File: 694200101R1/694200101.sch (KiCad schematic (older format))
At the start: 237 parts, among them J1 USB4085-GF-A, J2 Conn_01x02_Male, J3 Conn_01x02_Male, SW1 MX_SW, SW10 MX_SW, SW100 MX_SW, SW101 MX_SW, SW102 MX_SW, SW103 MX_SW, SW104 MX_SW, SW105 MX_SW, SW106 MX_SW, SW107 MX_SW, SW11 MX_SW, SW12 MX_SW, SW13 MX_SW, SW14 MX_SW, SW15 MX_SW, SW16 MX_SW, SW17 MX_SW, SW18 MX_SW, SW19 MX_SW, SW2 MX_SW, SW20 MX_SW, SW21 MX_SW, SW22 MX_SW, SW23 MX_SW, SW24 MX_SW, SW25 MX_SW, SW26 MX_SW, SW27 MX_SW, SW28 MX_SW, SW29 MX_SW, SW3 MX_SW, SW30 MX_SW, SW31 MX_SW, SW32 MX_SW, SW33 MX_SW, SW34 MX_SW, SW35 MX_SW, SW36 MX_SW, SW37 MX_SW, SW38 MX_SW, SW39 MX_SW, SW4 MX_SW, SW40 MX_SW, SW41 MX_SW, SW42 MX_SW, SW43 MX_SW, SW44 MX_SW, SW45 MX_SW, SW46 MX_SW, SW47 MX_SW, SW48 MX_SW, SW49 MX_SW, SW5 MX_SW, SW50 MX_SW, SW51 MX_SW, SW52 MX_SW, SW53 MX_SW, SW54 MX_SW, SW55 MX_SW, SW56 MX_SW, SW57 MX_SW, SW58 MX_SW, SW59 MX_SW, SW6 MX_SW, SW60 MX_SW, SW61 MX_SW, SW62 MX_SW, SW63 MX_SW, SW64 MX_SW, SW65 MX_SW, SW66 MX_SW, SW67 MX_SW, SW68 MX_SW, SW69 MX_SW, SW7 MX_SW, SW70 MX_SW, SW71 MX_SW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

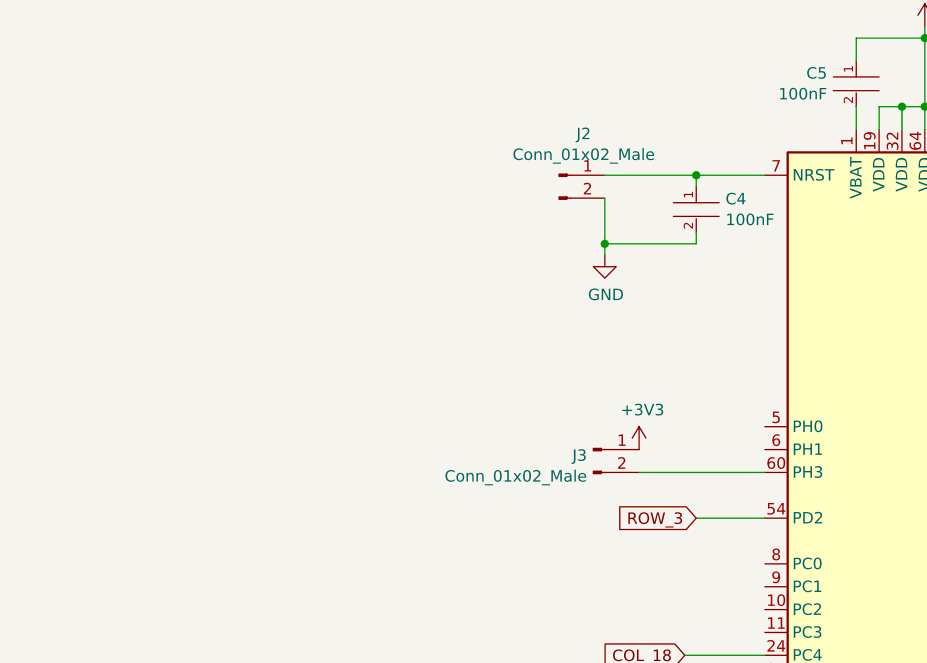
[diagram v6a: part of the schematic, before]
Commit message: Updated Schematic to use Crystal
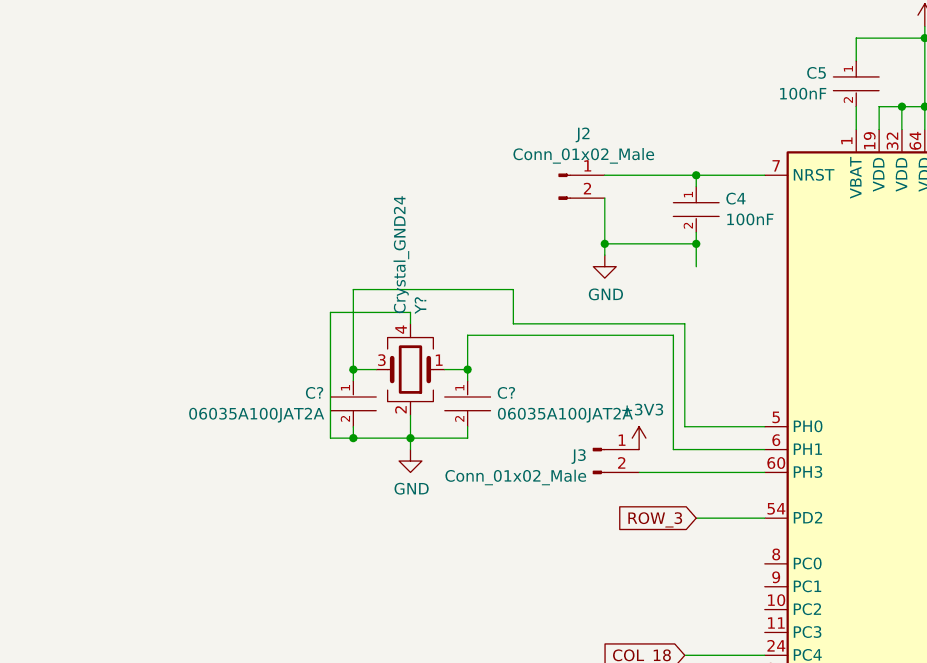
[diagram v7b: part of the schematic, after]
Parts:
- added C? (x2): 06035A100JAT2A, capacitor-lib:AVX-GRM124-0-0-IPC_C, symbol capacitor-lib:06035A100JAT2A
- added Y?: Crystal_GND24, symbol Device:Crystal_GND24
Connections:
- net GND: now also C?.2, C?.2, Y?.2, Y?.4
- net at U2.5 (PH0): now also C?.1, Y?.3
- net at U2.6 (PH1): now also C?.1, Y?.1
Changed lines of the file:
@@
 	1    0    0    -1
 $EndComp
-$Comp
-L MCU_ST_STM32L4:STM32L433RBTx U2
-U 1 1 5FE7C7AF
-P 8950 8200
-F 0 "U2" H 9200 6350 50  0000 C CNN
-F 1 "STM32L433RBTx" H 9450 6250 50  0000 C CNN
-F 2 "Package_QFP:LQFP-64_10x10mm_P0.5mm" H 8350 6500 50  0001 R CNN
-F 3 "http://www.st.com/st-web-ui/static/active/en/resource/technical/document/datasheet/DM00257192.pdf" H 8950 8200 50  0001 C CNN
-	1    8950 8200
-	1    0    0    -1
-$EndComp
 Wire Wire Line
 	8650 6100 8650 6000
@@
 	0    1    1    0
 $EndComp
-Wire Wire Line
-	9550 8900 10550 8900
-Wire Wire Line
-	9550 9000 10950 9000
 Text GLabel 11050 8900 2    50   Input ~ 0
 I2C_SCL
@@
 USB_D-
 Wire Wire Line
-	9550 7700 10000 7700
-Wire Wire Line
-	10000 7800 9550 7800
-Wire Wire Line
 	16050 6350 16050 6500
 Wire Wire Line
@@
 Text GLabel 16050 8700 3    50   Input ~ 0
 ENCODER_B
-Wire Wire Line
-	9550 8300 9900 8300
-Wire Wire Line
-	9550 8400 9900 8400
 Text GLabel 9900 8300 2    50   Input ~ 0
 ENCODER_A
@@
 Text GLabel 9900 8700 2    50   Input ~ 0
 ROW_1
-Wire Wire Line
-	9550 8800 9900 8800
-Wire Wire Line
-	9550 8700 9900 8700
-Wire Wire Line
-	9550 8600 9900 8600
 Text GLabel 9900 8600 2    50   Input ~ 0
 ROW_2
@@
 Text GLabel 7900 9300 0    50   Input ~ 0
 ROW_6
-Wire Wire Line
-	9550 8100 9900 8100
 Text GLabel 9900 8100 2    50   Input ~ 0
 COL_0
-Wire Wire Line
-	9550 8000 9900 8000
 Text GLabel 9900 8000 2    50   Input ~ 0
 COL_1
-Wire Wire Line
-	9550 7900 9900 7900
 Text GLabel 9900 7900 2    50   Input ~ 0
 COL_2
-Wire Wire Line
-	9550 7600 9900 7600
 Text GLabel 9900 7600 2    50   Input ~ 0
 COL_3
-Wire Wire Line
-	9550 7500 9900 7500
 Text GLabel 9900 7500 2    50   Input ~ 0
 COL_4
-Wire Wire Line
-	9550 7400 9900 7400
 Text GLabel 9900 7400 2    50   Input ~ 0
 COL_5
@@
 Text GLabel 7900 8900 0    50   Input ~ 0
 COL_9
-Wire Wire Line
-	9550 9800 9900 9800
 Text GLabel 9900 9800 2    50   Input ~ 0
 COL_10
-Wire Wire Line
-	9550 9700 9900 9700
 Text GLabel 9900 9700 2    50   Input ~ 0
 COL_11
-Wire Wire Line
-	9550 9600 9900 9600
 Text GLabel 9900 9600 2    50   Input ~ 0
 COL_12
-Wire Wire Line
-	9550 9500 9900 9500
 Text GLabel 9900 9500 2    50   Input ~ 0
 COL_13
-Wire Wire Line
-	9550 9400 9900 9400
 Text GLabel 9900 9400 2    50   Input ~ 0
 COL_14
-Wire Wire Line
-	9550 9300 9900 9300
 Text GLabel 9900 9300 2    50   Input ~ 0
 COL_15
-Wire Wire Line
-	9550 8500 9900 8500
 Text GLabel 9900 8500 2    50   Input ~ 0
 COL_16
@@
 Text GLabel 7900 8700 0    50   Input ~ 0
 COL_18
-Wire Wire Line
-	9550 7300 9900 7300
 Text GLabel 9900 7300 2    50   Input ~ 0
 COL_19
-Wire Wire Line
-	9550 7200 9900 7200
 Text GLabel 9900 7200 2    50   Input ~ 0
 COL_20
-Wire Wire Line
-	9550 7100 9900 7100
 Text GLabel 9900 7100 2    50   Input ~ 0
 COL_21
-Wire Wire Line
-	9550 7000 9900 7000
 Text GLabel 9900 7000 2    50   Input ~ 0
 COL_22
@@
 Wire Wire Line
 	4500 7550 4500 7500
+$Comp
+L capacitor-lib:06035A100JAT2A C?
+U 1 1 5FF44365
+P 6950 7700
+F 0 "C?" H 6822 7554 50  0000 R CNN
+F 1 "06035A100JAT2A" H 6822 7645 50  0000 R CNN
+F 2 "capacitor-lib:AVX-GRM124-0-0-IPC_C" H 6950 8000 50  0001 L CNN
+F 3 "https://search.murata.co.jp/Ceramy/image/img/A01X/G101/ENG/GRM1885C1E472JA01-01A.pdf" H 6950 8100 50  0001 L CNN
+F 4 "10pF" H 6950 8200 50  0001 L CNN "capacitance"
+F 5 "Cap" H 6950 8300 50  0001 L CNN "category"
+F 6 "Passive Components" H 6950 8400 50  0001 L CNN "device class L1"
+F 7 "Capacitors" H 6950 8500 50  0001 L CNN "device class L2"
+F 8 "Ceramic Capacitors" H 6950 8600 50  0001 L CNN "device class L3"
+F 9 "CAP CER 10PF 50V C0G/NP0 0603" H 6950 8700 50  0001 L CNN "digikey description"
+F 10 "478-1163-2-ND" H 6950 8800 50  0001 L CNN "digikey part number"
+F 11 "0.9mm" H 6950 8900 50  0001 L CNN "height"
+F 12 "CAPC16080X186" H 6950 9000 50  0001 L CNN "ipc land pattern name"
+F 13 "yes" H 6950 9100 50  0001 L CNN "lead free"
+F 14 "936bf8fcd50e4ef0" H 6950 9200 50  0001 L CNN "library id"
+F 15 "AVX" H 6950 9300 50  0001 L CNN "manufacturer"
+F 16 "Ceramic" H 6950 9400 50  0001 L CNN "material"
+F 17 "0603 10 pF 50 V ±5 % Tol. C0G/NP0 Surface Mount Multilayer Ceramic Capacitor" H 6950 9500 50  0001 L CNN "mouser description"
+F 18 "581-06035A100J" H 6950 9600 50  0001 L CNN "mouser part number"
+F 19 "0603" H 6950 9700 50  0001 L CNN "package"
+F 20 "yes" H 6950 9800 50  0001 L CNN "rohs"
+F 21 "0mm" H 6950 9900 50  0001 L CNN "standoff height"
+F 22 "C0G" H 6950 10000 50  0001 L CNN "temperature characteristic"
+F 23 "+125°C" H 6950 10100 50  0001 L CNN "temperature range high"
+F 24 "-55°C" H 6950 10200 50  0001 L CNN "temperature range low"
+F 25 "5%" H 6950 10300 50  0001 L CNN "tolerance"
+F 26 "50V" H 6950 10400 50  0001 L CNN "voltage rating"
+	1    6950 7700
+	-1   0    0    1
+$EndComp
+Wire Wire Line
+	9550 9000 10950 9000
+Wire Wire Line
+	9550 8900 10550 8900
+Wire Wire Line
+	9550 8800 9900 8800
+Wire Wire Line
+	9550 8700 9900 8700
+Wire Wire Line
+	9550 8600 9900 8600
+Wire Wire Line
+	9550 8500 9900 8500
+Wire Wire Line
+	9550 9800 9900 9800
+Wire Wire Line
+	9550 9700 9900 9700
+Wire Wire Line
+	9550 9600 9900 9600
+Wire Wire Line
+	9550 9500 9900 9500
+Wire Wire Line
+	9550 9400 9900 9400
+Wire Wire Line
+	9550 9300 9900 9300
+Wire Wire Line
+	9550 8400 9900 8400
+Wire Wire Line
+	9550 8300 9900 8300
+Wire Wire Line
+	9550 7500 9900 7500
+Wire Wire Line
+	9550 7400 9900 7400
+Wire Wire Line
+	9550 7300 9900 7300
+Wire Wire Line
+	9550 7200 9900 7200
+Wire Wire Line
+	9550 7100 9900 7100
+Wire Wire Line
+	9550 7000 9900 7000
+Wire Wire Line
+	9550 8100 9900 8100
+Wire Wire Line
+	9550 8000 9900 8000
+Wire Wire Line
+	9550 7900 9900 7900
+Wire Wire Line
+	10000 7800 9550 7800
+Wire Wire Line
+	9550 7700 10000 7700
+Wire Wire Line
+	9550 7600 9900 7600
+Wire Wire Line
+	7950 7000 7950 6900
+Connection ~ 7950 6900
+$Comp
+L MCU_ST_STM32L4:STM32L433RBTx U2
+U 1 1 5FE7C7AF
+P 8950 8200
+F 0 "U2" H 9200 6350 50  0000 C CNN
+F 1 "STM32L433RBTx" H 9450 6250 50  0000 C CNN
+F 2 "Package_QFP:LQFP-64_10x10mm_P0.5mm" H 8350 6500 50  0001 R CNN
+F 3 "http://www.st.com/st-web-ui/static/active/en/resource/technical/document/datasheet/DM00257192.pdf" H 8950 8200 50  0001 C CNN
+	1    8950 8200
+	1    0    0    -1
+$EndComp
+$Comp
+L capacitor-lib:06035A100JAT2A C?
+U 1 1 60087526
+P 6450 7700
+F 0 "C?" H 6577 7554 50  0000 L CNN
+F 1 "06035A100JAT2A" H 6577 7645 50  0000 L CNN
+F 2 "capacitor-lib:AVX-GRM124-0-0-IPC_C" H 6450 8000 50  0001 L CNN
+F 3 "https://search.murata.co.jp/Ceramy/image/img/A01X/G101/ENG/GRM1885C1E472JA01-01A.pdf" H 6450 8100 50  0001 L CNN
+F 4 "10pF" H 6450 8200 50  0001 L CNN "capacitance"
+F 5 "Cap" H 6450 8300 50  0001 L CNN "category"
+F 6 "Passive Components" H 6450 8400 50  0001 L CNN "device class L1"
+F 7 "Capacitors" H 6450 8500 50  0001 L CNN "device class L2"
+F 8 "Ceramic Capacitors" H 6450 8600 50  0001 L CNN "device class L3"
+F 9 "CAP CER 10PF 50V C0G/NP0 0603" H 6450 8700 50  0001 L CNN "digikey description"
+F 10 "478-1163-2-ND" H 6450 8800 50  0001 L CNN "digikey part number"
+F 11 "0.9mm" H 6450 8900 50  0001 L CNN "height"
+F 12 "CAPC16080X186" H 6450 9000 50  0001 L CNN "ipc land pattern name"
+F 13 "yes" H 6450 9100 50  0001 L CNN "lead free"
+F 14 "936bf8fcd50e4ef0" H 6450 9200 50  0001 L CNN "library id"
+F 15 "AVX" H 6450 9300 50  0001 L CNN "manufacturer"
+F 16 "Ceramic" H 6450 9400 50  0001 L CNN "material"
+F 17 "0603 10 pF 50 V ±5 % Tol. C0G/NP0 Surface Mount Multilayer Ceramic Capacitor" H 6450 9500 50  0001 L CNN "mouser description"
+F 18 "581-06035A100J" H 6450 9600 50  0001 L CNN "mouser part number"
+F 19 "0603" H 6450 9700 50  0001 L CNN "package"
+F 20 "yes" H 6450 9800 50  0001 L CNN "rohs"
+F 21 "0mm" H 6450 9900 50  0001 L CNN "standoff height"
+F 22 "C0G" H 6450 10000 50  0001 L CNN "temperature characteristic"
+F 23 "+125°C" H 6450 10100 50  0001 L CNN "temperature range high"
+F 24 "-55°C" H 6450 10200 50  0001 L CNN "temperature range low"
+F 25 "5%" H 6450 10300 50  0001 L CNN "tolerance"
+F 26 "50V" H 6450 10400 50  0001 L CNN "voltage rating"
+	1    6450 7700
+	-1   0    0    1
+$EndComp
+Wire Wire Line
+	6450 7700 6450 7750
+Wire Wire Line
+	6450 7750 6700 7750
+Wire Wire Line
+	6700 7750 6700 7650
+Wire Wire Line
+	6700 7750 6950 7750
+Wire Wire Line
+	6950 7750 6950 7700
+Connection ~ 6700 7750
+Wire Wire Line
+	6450 7500 6450 7450
+Wire Wire Line
+	6450 7450 6550 7450
+Wire Wire Line
+	6850 7450 6950 7450
+Wire Wire Line
+	6950 7450 6950 7500
+Wire Wire Line
+	6450 7750 6350 7750
+Connection ~ 6450 7750
+$Comp
+L Device:Crystal_GND24 Y?
+U 1 1 60782252
+P 6700 7450
+F 0 "Y?" V 6654 7207 50  0000 R CNN
+F 1 "Crystal_GND24" V 6745 7207 50  0000 R CNN
+F 2 "" H 6700 7450 50  0001 C CNN
+F 3 "~" H 6700 7450 50  0001 C CNN
+	1    6700 7450
+	-1   0    0    1
+$EndComp
+Wire Wire Line
+	6350 7200 6700 7200
+Wire Wire Line
+	6700 7200 6700 7250
+Wire Wire Line
+	6350 7200 6350 7750
+Wire Wire Line
+	6450 7450 6450 7100
+Wire Wire Line
+	6450 7100 7150 7100
+Wire Wire Line
+	7150 7100 7150 7250
+Connection ~ 6450 7450
+Wire Wire Line
+	6950 7450 6950 7300
+Wire Wire Line
+	6950 7300 7850 7300
+Wire Wire Line
+	7850 7300 7850 7800
+Wire Wire Line
+	7850 7800 8250 7800
+Connection ~ 6950 7450
+Wire Wire Line
+	7150 7250 7900 7250
+Wire Wire Line
+	7900 7250 7900 7700
+Wire Wire Line
+	7900 7700 8250 7700
+$Comp
+L power:GND #PWR?
+U 1 1 6065E993
+P 6700 7800
+F 0 "#PWR?" H 6700 7550 50  0001 C CNN
+F 1 "GND" H 6705 7627 50  0000 C CNN
+F 2 "" H 6700 7800 50  0001 C CNN
+F 3 "" H 6700 7800 50  0001 C CNN
+	1    6700 7800
+	1    0    0    -1
+$EndComp
+Wire Wire Line
+	6700 7750 6700 7800
 $EndSCHEMATC

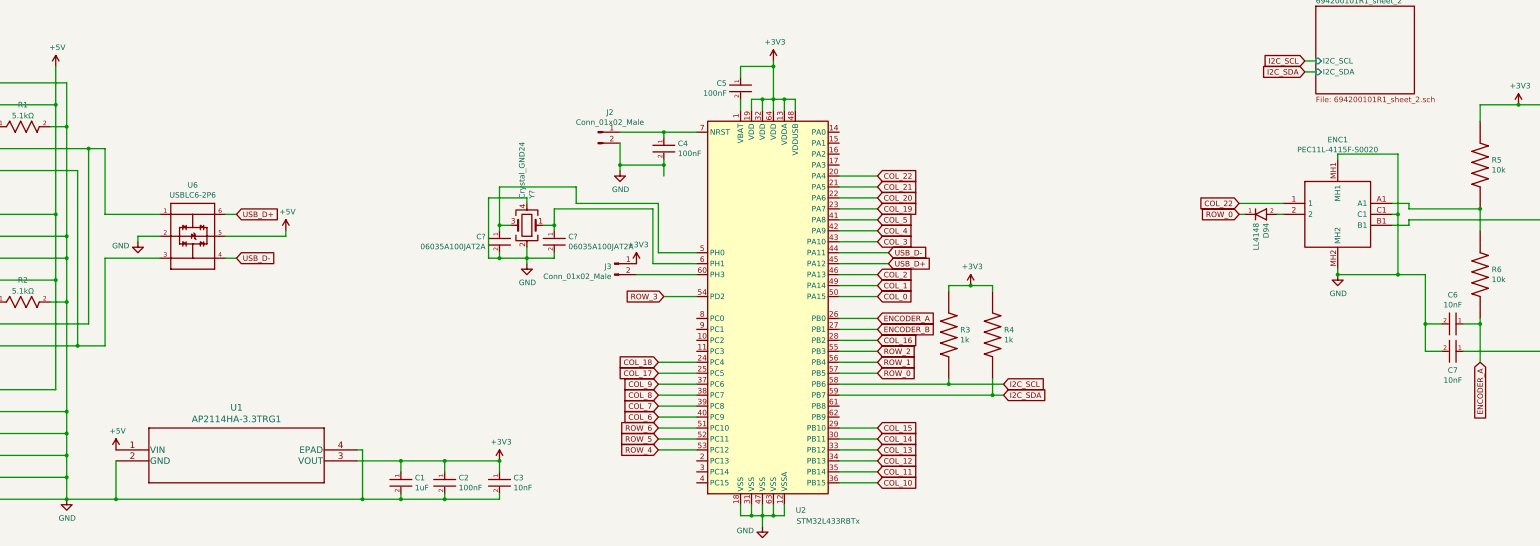
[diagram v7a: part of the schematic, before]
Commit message: diodes laidout
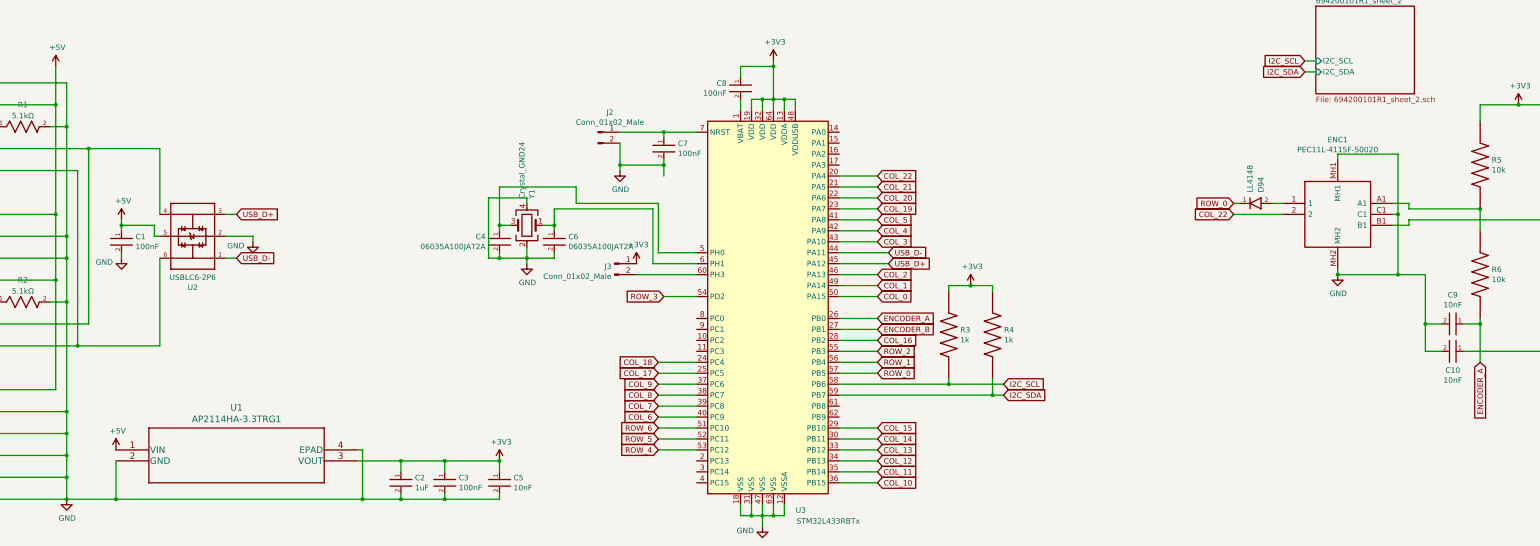
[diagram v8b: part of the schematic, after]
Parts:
- added C1: CL10B104KB8NNNL, capacitor-lib:Samsung-CL10-09_2006-0-IPC_C, symbol capacitor-lib:CL10B104KB8NNNL
- gave numbers to parts that had none: 3
- renumbered C7 to C10, C1 to C2, C2 to C3, C3 to C5, C4 to C7, C5 to C8, C6 to C9, U6 to U2, U2 to U3
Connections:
- net +5V: now also C1.1
- net COL_22: now also ENC1.2; no longer ENC1.1
- net GND: now also C1.2
- net USB_D+: now also U2.3; no longer U2.6
- net USB_D-: now also U2.1; no longer U2.4
- net at J1.A6 (Dp1), J1.B6 (Dp2): now also U2.4; no longer U2.1
- net at J1.A7 (Dn1), J1.B7 (Dn2): now also U2.6; no longer U2.3
- net at D94.2 (ANODE): now also ENC1.1; no longer ENC1.2
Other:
- moved on the sheet: D94
